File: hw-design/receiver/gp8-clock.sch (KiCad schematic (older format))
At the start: 50 parts, among them J1 CONN_01X01, J10 CONN_01X01, J11 CONN_01X01, J12 CONN_01X01, J2 CONN_01X01, J3 CONN_01X01, J4 CONN_01X01, J5 CONN_01X01, J6 CONN_01X01, J7 CONN_01X01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

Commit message: Pre refactoring functionality restored
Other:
- note added: "Uwaga na pinout, bo każdy receiver ma inny!!\nMontaż po stronie komponentów (nie ekranu).\nDobre : TSOP39138\nZłe : TSOP39538"
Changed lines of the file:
@@
 NoConn ~ 950  3125
 NoConn ~ 950  3275
+Text Notes 800  5375 0    60   ~ 0
+Uwaga na pinout, bo każdy receiver ma inny!!\nMontaż po stronie komponentów (nie ekranu).\nDobre : TSOP39138\nZłe : TSOP39538
 $EndSCHEMATC

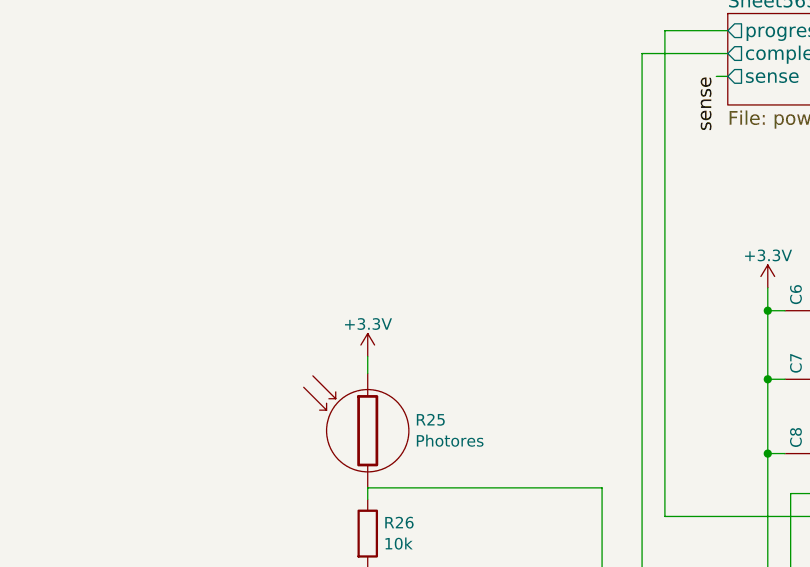
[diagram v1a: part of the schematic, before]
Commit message: Backlight and battery monotoring. Faulty start/stop mehcanism
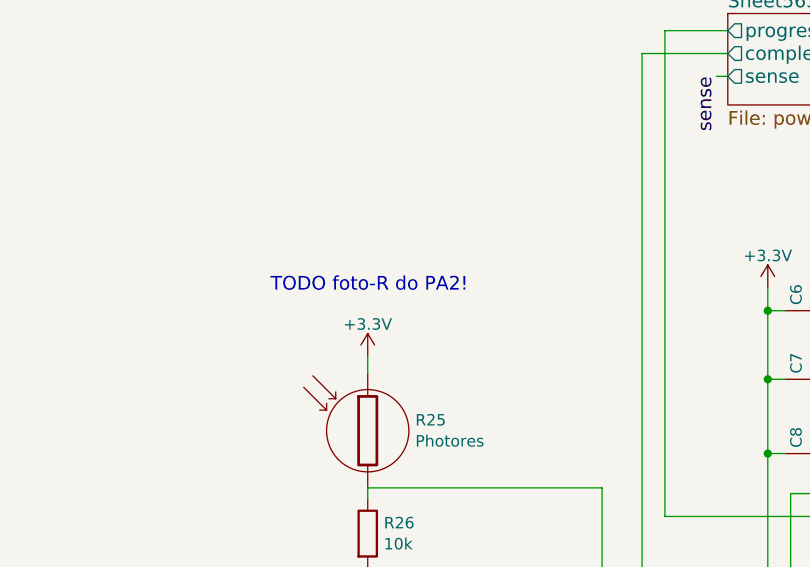
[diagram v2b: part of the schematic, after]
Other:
- note added: "TODO foto-R do PA2!"
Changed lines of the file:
@@
 Text Notes 800  5375 0    60   ~ 0
 Uwaga na pinout, bo każdy receiver ma inny!!\nMontaż po stronie komponentów (nie ekranu).\nDobre : TSOP39138\nZłe : TSOP39538
+Text Notes 3825 2075 0    60   ~ 0
+TODO foto-R do PA2!
 $EndSCHEMATC

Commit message: Many changes
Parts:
- removed J1, J10, J11, J12: CONN_01X01, Mounting_Holes:MountingHole_3.2mm_M3_DIN965_Pad, symbol CONN_01X01
- removed J2, J3, J4, J5, J6, J7, J8, J9: CONN_01X01, Pin_Headers:Pin_Header_Straight_1x01_Pitch2.00mm, symbol CONN_01X01
- added BT1: Battery, Connector_PinHeader_2.54mm:PinHeader_1x02_P2.54mm_Vertical, symbol Device:Battery
- added C15: 100nF, Capacitor_SMD:C_0603_1608Metric, symbol gp8-clock-rescue:C-RESCUE-gp8-clock
- added C16: 1µF, Capacitor_SMD:C_0603_1608Metric, symbol Device:C
- added D10, D3, D4, D5, D6, D7, D8, D9: LED, LED_SMD:LED_0805_2012Metric, symbol gp8-clock-rescue:LED-RESCUE-gp8-clock
- added Q2, Q4: BC847, Package_TO_SOT_SMD:SOT-23, symbol Device:Q_NPN_BEC
- added R2: 1k, Resistor_SMD:R_0603_1608Metric, symbol gp8-clock-rescue:R-RESCUE-gp8-clock
- added R4: 220, Resistor_SMD:R_0603_1608Metric, symbol gp8-clock-rescue:R-RESCUE-gp8-clock
- added RV1: 47R, Potentiometer_THT:Potentiometer_ACP_CA9-H5_Horizontal, symbol Device:POT
- added SW2: SW_SPDT, symbol Switch:SW_SPDT
- added U2: EDS809-1-lcd, symbol iwasz-kicad:EDS809-1-lcd
- added U5: HT1621B, symbol iwasz-kicad:HT1621B
- C1, C10, C12, C13, C2, C3, C4, C5, C7, C8, C9: footprint w_smd_cap:c_0603 -> Capacitor_SMD:C_0603_1608Metric; symbol C -> gp8-clock-rescue:C-RESCUE-gp8-clock
- C11, C14, C6: symbol C -> gp8-clock-rescue:C-RESCUE-gp8-clock
- D1: symbol LED -> gp8-clock-rescue:LED-RESCUE-gp8-clock
- P2: symbol test-double -> iwasz-kicad:test-double
- P3, P6: footprint w_pin_strip:pin_strip_2mm_4 -> Connector_PinHeader_2.00mm:PinHeader_1x04_P2.00mm_Vertical; symbol CONN_01X04 -> gp8-clock-rescue:CONN_01X04-RESCUE-gp8-clock
- Q1, Q3: footprint w_smd_trans:sot23 -> Package_TO_SOT_SMD:SOT-23; symbol Q_NPN_BCE -> Device:Q_NPN_BEC
- R1, R13, R22, R23, R24, R26, R27, R3, R31, R32, R9: footprint w_smd_resistors:r_0603 -> Resistor_SMD:R_0603_1608Metric; symbol R -> gp8-clock-rescue:R-RESCUE-gp8-clock
- R25: symbol Photores -> gp8-clock-rescue:Photores-RESCUE-gp8-clock
- SP1: footprint Buzzers_Beepers:Buzzer_12x9.5RM7.6 -> Buzzer_Beeper:Buzzer_12x9.5RM7.6; symbol SPEAKER -> gp8-clock-rescue:SPEAKER-RESCUE-gp8-clock
- SW1: symbol SW_PUSH -> gp8-clock-rescue:SW_PUSH-RESCUE-gp8-clock
- U1: symbol TSOP39538 -> iwasz-kicad:TSOP39538
- U3: symbol STM32F0-LQFP48 -> iwasz-kicad:STM32F0-LQFP48
- U4: symbol usb-micro -> iwasz-kicad:usb-micro
- Y1: symbol Crystal -> gp8-clock-rescue:Crystal-RESCUE-gp8-clock
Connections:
- net labels added: CS, DATA, WR, ambient
- net labels removed: +BATT, sense
- wire segments 118 -> 242
- no-connect marks 33 -> 47
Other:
- note added: "1.4V"
- note added: "2.1V"
- note added: "22R -> 65mA"
- note added: "2V"
- note added: "9.5mA"
- note added: "90mV typ"
- note added: "A"
- note added: "B"
- note removed: "TODO foto-R do PA2!"
- moved on the sheet: C10, C11, C12, C13, C14, C2, C3, C4, C5, C6, C7, C8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
